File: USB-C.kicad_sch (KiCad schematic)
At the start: 2 parts, among them P1 USB_C_Plug_USB2.0

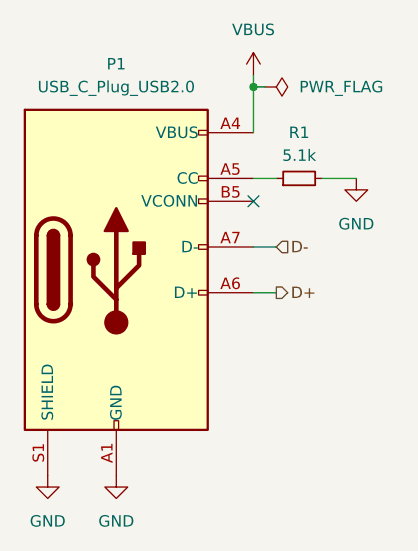
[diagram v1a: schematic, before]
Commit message: BMS updates
Added missing capacitor for OTG
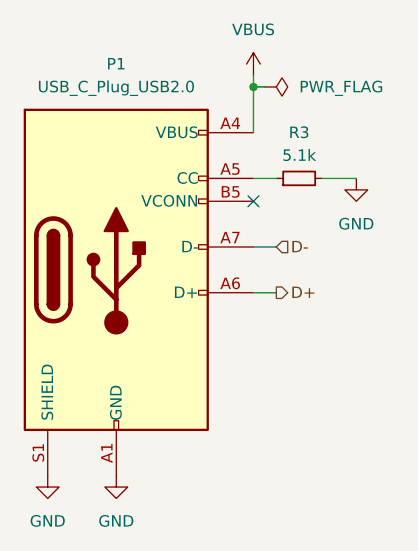
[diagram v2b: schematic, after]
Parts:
- renumbered R1 to R3
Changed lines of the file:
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@@
 		(dnp no)
 		(fields_autoplaced yes)
-		(property "Reference" "#PWR0103"
+		(property "Reference" "#PWR019"
 			(at 133.35 62.23 0)
 			(effects
@@
 			(project "Minibadge Display 5x3"
 				(path "/e5119d15-74fb-4259-abbc-5cab1f368532/f82e88ca-9adc-48b9-bd3d-d05196ebe384"
-					(reference "#PWR0103")
+					(reference "#PWR019")
 					(unit 1)
 				)
@@
 		(dnp no)
 		(fields_autoplaced yes)
-		(property "Reference" "#FLG01"
+		(property "Reference" "#FLG04"
 			(at 125.095 45.72 0)
 			(effects
@@
 			(project "Minibadge Display 5x3"
 				(path "/e5119d15-74fb-4259-abbc-5cab1f368532/f82e88ca-9adc-48b9-bd3d-d05196ebe384"
-					(reference "#FLG01")
+					(reference "#FLG04")
 					(unit 1)
 				)
@@
 		(dnp no)
 		(fields_autoplaced yes)
-		(property "Reference" "#PWR0102"
+		(property "Reference" "#PWR018"
 			(at 121.92 48.26 0)
 			(effects
@@
 			(project "Minibadge Display 5x3"
 				(path "/e5119d15-74fb-4259-abbc-5cab1f368532/f82e88ca-9adc-48b9-bd3d-d05196ebe384"
-					(reference "#PWR0102")
+					(reference "#PWR018")
 					(unit 1)
 				)
@@
 		(on_board yes)
 		(dnp no)
-		(property "Reference" "R1"
+		(property "Reference" "R3"
 			(at 127 50.8 90)
 			(effects
@@
 			(project "Minibadge Display 5x3"
 				(path "/e5119d15-74fb-4259-abbc-5cab1f368532/f82e88ca-9adc-48b9-bd3d-d05196ebe384"
-					(reference "R1")
+					(reference "R3")
 					(unit 1)
 				)
@@
 		(dnp no)
 		(fields_autoplaced yes)
-		(property "Reference" "#PWR0101"
+		(property "Reference" "#PWR017"
 			(at 106.68 95.25 0)
 			(effects
@@
 			(project "Minibadge Display 5x3"
 				(path "/e5119d15-74fb-4259-abbc-5cab1f368532/f82e88ca-9adc-48b9-bd3d-d05196ebe384"
-					(reference "#PWR0101")
+					(reference "#PWR017")
 					(unit 1)
 				)
@@
 		(dnp no)
 		(fields_autoplaced yes)
-		(property "Reference" "#PWR0100"
+		(property "Reference" "#PWR016"
 			(at 99.06 95.25 0)
 			(effects
@@
 			(project "Minibadge Display 5x3"
 				(path "/e5119d15-74fb-4259-abbc-5cab1f368532/f82e88ca-9adc-48b9-bd3d-d05196ebe384"
-					(reference "#PWR0100")
-					(unit 1)
-				)
+					(reference "#PWR016")
+					(unit 1)
+				)
